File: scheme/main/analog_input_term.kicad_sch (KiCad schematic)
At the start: 2 parts, among them J3 Conn_01x03

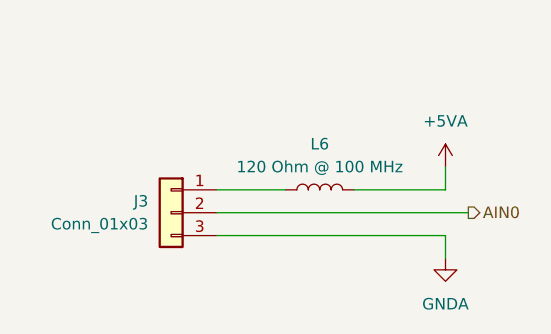
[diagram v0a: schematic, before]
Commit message: analog input 0 schematic modified
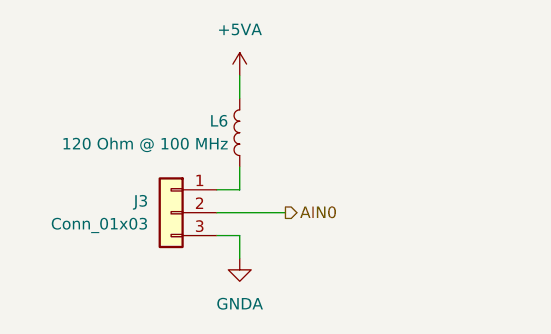
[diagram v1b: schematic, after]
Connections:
- net +5VA: now also L6.1; no longer L6.2
- net at J3.1 (Pin_1): now also L6.2; no longer L6.1
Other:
- moved on the sheet: L6
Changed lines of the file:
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@@
 	(wire
 		(pts
-			(xy 157.48 88.9) (xy 157.48 91.44)
-		)
-		(stroke
-			(width 0)
-			(type default)
-		)
-	)
-	(wire
-		(pts
-			(xy 132.08 93.98) (xy 160.02 93.98)
-		)
-		(stroke
-			(width 0)
-			(type default)
-		)
-	)
-	(wire
-		(pts
-			(xy 132.08 96.52) (xy 157.48 96.52)
-		)
-		(stroke
-			(width 0)
-			(type default)
-		)
-	)
-	(wire
-		(pts
-			(xy 147.32 91.44) (xy 157.48 91.44)
-		)
-		(stroke
-			(width 0)
-			(type default)
-		)
-	)
-	(wire
-		(pts
-			(xy 157.48 99.06) (xy 157.48 96.52)
-		)
-		(stroke
-			(width 0)
-			(type default)
-		)
-	)
-	(wire
-		(pts
-			(xy 132.08 91.44) (xy 139.7 91.44)
+			(xy 134.62 81.28) (xy 134.62 78.74)
+		)
+		(stroke
+			(width 0)
+			(type default)
+		)
+	)
+	(wire
+		(pts
+			(xy 134.62 88.9) (xy 134.62 91.44)
+		)
+		(stroke
+			(width 0)
+			(type default)
+		)
+	)
+	(wire
+		(pts
+			(xy 132.08 93.98) (xy 139.7 93.98)
+		)
+		(stroke
+			(width 0)
+			(type default)
+		)
+	)
+	(wire
+		(pts
+			(xy 132.08 96.52) (xy 134.62 96.52)
+		)
+		(stroke
+			(width 0)
+			(type default)
+		)
+	)
+	(wire
+		(pts
+			(xy 134.62 91.44) (xy 132.08 91.44)
+		)
+		(stroke
+			(width 0)
+			(type default)
+		)
+	)
+	(wire
+		(pts
+			(xy 134.62 99.06) (xy 134.62 96.52)
 		)
 		(stroke
@@
 	(hierarchical_label "AIN0"
 		(shape output)
-		(at 160.02 93.98 0)
+		(at 139.7 93.98 0)
 		(effects
 			(font
@@
 	(symbol
 		(lib_id "Device:L")
-		(at 143.51 91.44 90)
+		(at 134.62 85.09 0)
+		(mirror y)
 		(unit 1)
 		(exclude_from_sim no)
@@
 		(on_board yes)
 		(dnp no)
-		(fields_autoplaced yes)
 		(property "Reference" "L6"
-			(at 143.51 86.36 90)
-			(effects
-				(font
-					(size 1.27 1.27)
-				)
+			(at 133.35 83.8199 0)
+			(effects
+				(font
+					(size 1.27 1.27)
+				)
+				(justify left)
 			)
 		)
 		(property "Value" "120 Ohm @ 100 MHz"
-			(at 143.51 88.9 90)
-			(effects
-				(font
-					(size 1.27 1.27)
-				)
+			(at 133.35 86.3599 0)
+			(effects
+				(font
+					(size 1.27 1.27)
+				)
+				(justify left)
 			)
 		)
 		(property "Footprint" "Inductor_SMD:L_0805_2012Metric"
-			(at 143.51 91.44 0)
+			(at 134.62 85.09 0)
 			(effects
 				(font
@@
 		)
 		(property "Datasheet" "~"
-			(at 143.51 91.44 0)
+			(at 134.62 85.09 0)
 			(effects
 				(font
@@
 		)
 		(property "Description" "BLM21PG121SN1D"
-			(at 143.51 91.44 0)
+			(at 134.62 85.09 0)
 			(effects
 				(font
@@
 	(symbol
 		(lib_id "power:GNDA")
-		(at 157.48 99.06 0)
+		(at 134.62 99.06 0)
 		(unit 1)
 		(exclude_from_sim no)
@@
 		(fields_autoplaced yes)
 		(property "Reference" "#PWR18"
-			(at 157.48 105.41 0)
+			(at 134.62 105.41 0)
 			(effects
 				(font
@@
 		)
 		(property "Value" "GNDA"
-			(at 157.48 104.14 0)
+			(at 134.62 104.14 0)
 			(effects
 				(font
@@
 		)
 		(property "Footprint" ""
-			(at 157.48 99.06 0)
+			(at 134.62 99.06 0)
 			(effects
 				(font
@@
 		)
 		(property "Datasheet" ""
-			(at 157.48 99.06 0)
+			(at 134.62 99.06 0)
 			(effects
 				(font
@@
 		)
 		(property "Description" "Power symbol creates a global label with name \"GNDA\" , analog ground"
-			(at 157.48 99.06 0)
+			(at 134.62 99.06 0)
 			(effects
 				(font
@@
 	(symbol
 		(lib_id "power:+5VA")
-		(at 157.48 88.9 0)
+		(at 134.62 78.74 0)
 		(unit 1)
 		(exclude_from_sim no)
@@
 		(fields_autoplaced yes)
 		(property "Reference" "#PWR19"
-			(at 157.48 92.71 0)
+			(at 134.62 82.55 0)
 			(effects
 				(font
@@
 		)
 		(property "Value" "+5VA"
-			(at 157.48 83.82 0)
+			(at 134.62 73.66 0)
 			(effects
 				(font
@@
 		)
 		(property "Footprint" ""
-			(at 157.48 88.9 0)
+			(at 134.62 78.74 0)
 			(effects
 				(font
@@
 		)
 		(property "Datasheet" ""
-			(at 157.48 88.9 0)
+			(at 134.62 78.74 0)
 			(effects
 				(font
@@
 		)
 		(property "Description" "Power symbol creates a global label with name \"+5VA\""
-			(at 157.48 88.9 0)
-			(effects
-				(font
+			(at 134.62 78.74 0)
+			(effects
+				(font
